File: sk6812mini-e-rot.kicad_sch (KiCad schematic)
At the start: 2 parts

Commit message: finish routing
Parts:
- LED1: footprint PCM_marbastlib-mx:LED_MX_6028R-ROT -> MoonBoard:SK 6812 MINI-EA-ROT
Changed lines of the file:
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@@
       (effects (font (size 1.27 1.27)))
     )
-    (property "Footprint" "PCM_marbastlib-mx:LED_MX_6028R-ROT" (at 41.91 40.005 0)
+    (property "Footprint" "MoonBoard:SK 6812 MINI-EA-ROT" (at 41.91 40.005 0)
       (effects (font (size 1.27 1.27)) hide)
     )

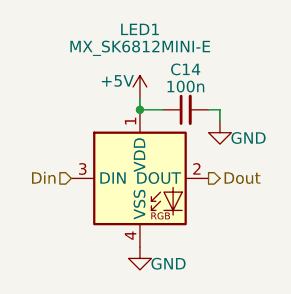
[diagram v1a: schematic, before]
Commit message: fix LED footprint, add boot/reset jumpers
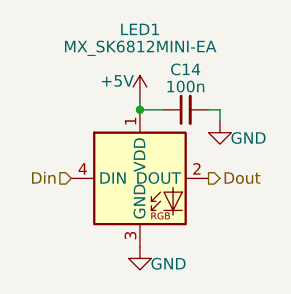
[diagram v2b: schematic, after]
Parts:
- LED1: value MX_SK6812MINI-E -> MX_SK6812MINI-EA; symbol PCM_marbastlib-mx:MX_SK6812MINI-E -> MoonBoard:MX_SK6812MINI-EA
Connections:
- net Din: now also LED1.4 (DIN); no longer LED1.3 (DIN)
- net GND: now also LED1.3 (GND); no longer LED1.4 (VSS)
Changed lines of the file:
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@@
     )
   )
-  (symbol (lib_id "PCM_marbastlib-mx:MX_SK6812MINI-E") (at 41.91 40.005 0) (unit 1)
+  (symbol (lib_id "MoonBoard:MX_SK6812MINI-EA") (at 41.91 40.005 0) (unit 1)
     (in_bom yes) (on_board yes) (dnp no)
     (property "Reference" "LED1" (at 41.91 23.495 0)
       (effects (font (size 1.27 1.27)))
     )
-    (property "Value" "MX_SK6812MINI-E" (at 41.91 25.4 0)
+    (property "Value" "MX_SK6812MINI-EA" (at 41.91 25.4 0)
       (effects (font (size 1.27 1.27)))
     )
-    (property "Footprint" "MoonBoard:SK 6812 MINI-EA-ROT" (at 41.91 40.005 0)
+    (property "Footprint" "MoonBoard:SK 6812 MINI-EA-ROT" (at 41.91 59.055 0)
       (effects (font (size 1.27 1.27)) hide)
     )

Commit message: add reverse polarity protection to LDO
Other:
- title: (none) -> MoonBoard
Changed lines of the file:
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@@
 (kicad_sch (version 20230121) (generator eeschema)
   (paper "A4")
+  (title_block
+    (title "MoonBoard")
+  )
   (junction (at 41.91 32.385) (diameter 0) (color 0 0 0 0)
   )

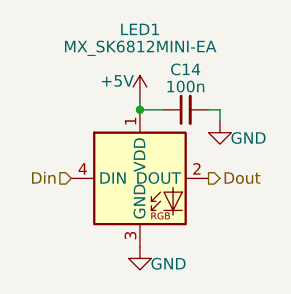
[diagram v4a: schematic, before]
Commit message: update to kicad 8
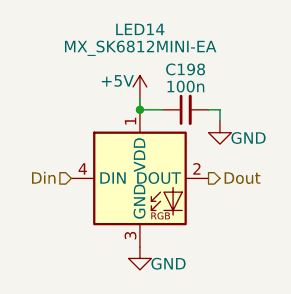
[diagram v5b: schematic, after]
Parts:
- renumbered C14 to C198, LED1 to LED14
